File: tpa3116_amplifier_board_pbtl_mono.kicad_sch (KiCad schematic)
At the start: 47 parts, among them IC1 TPA3116D2QDADRQ1, J1 power_supply, J2 Conn_01x04, J3 power_supply, J4 output_right

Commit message: заменил конденсаторы C1, С2 на smd
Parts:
- C1, C2: footprint Capacitor_THT:C_Rect_L7.0mm_W4.5mm_P5.00mm -> Capacitor_SMD:C_0805_2012Metric

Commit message: изменил номинал конденсатора C3
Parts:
- C3: value 1u -> --
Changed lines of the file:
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@@
       (effects (font (size 1.27 1.27)))
     )
-    (property "Value" "1u" (at 58.42 66.04 90)
+    (property "Value" "--" (at 58.42 66.04 90)
       (effects (font (size 1.27 1.27)))
     )

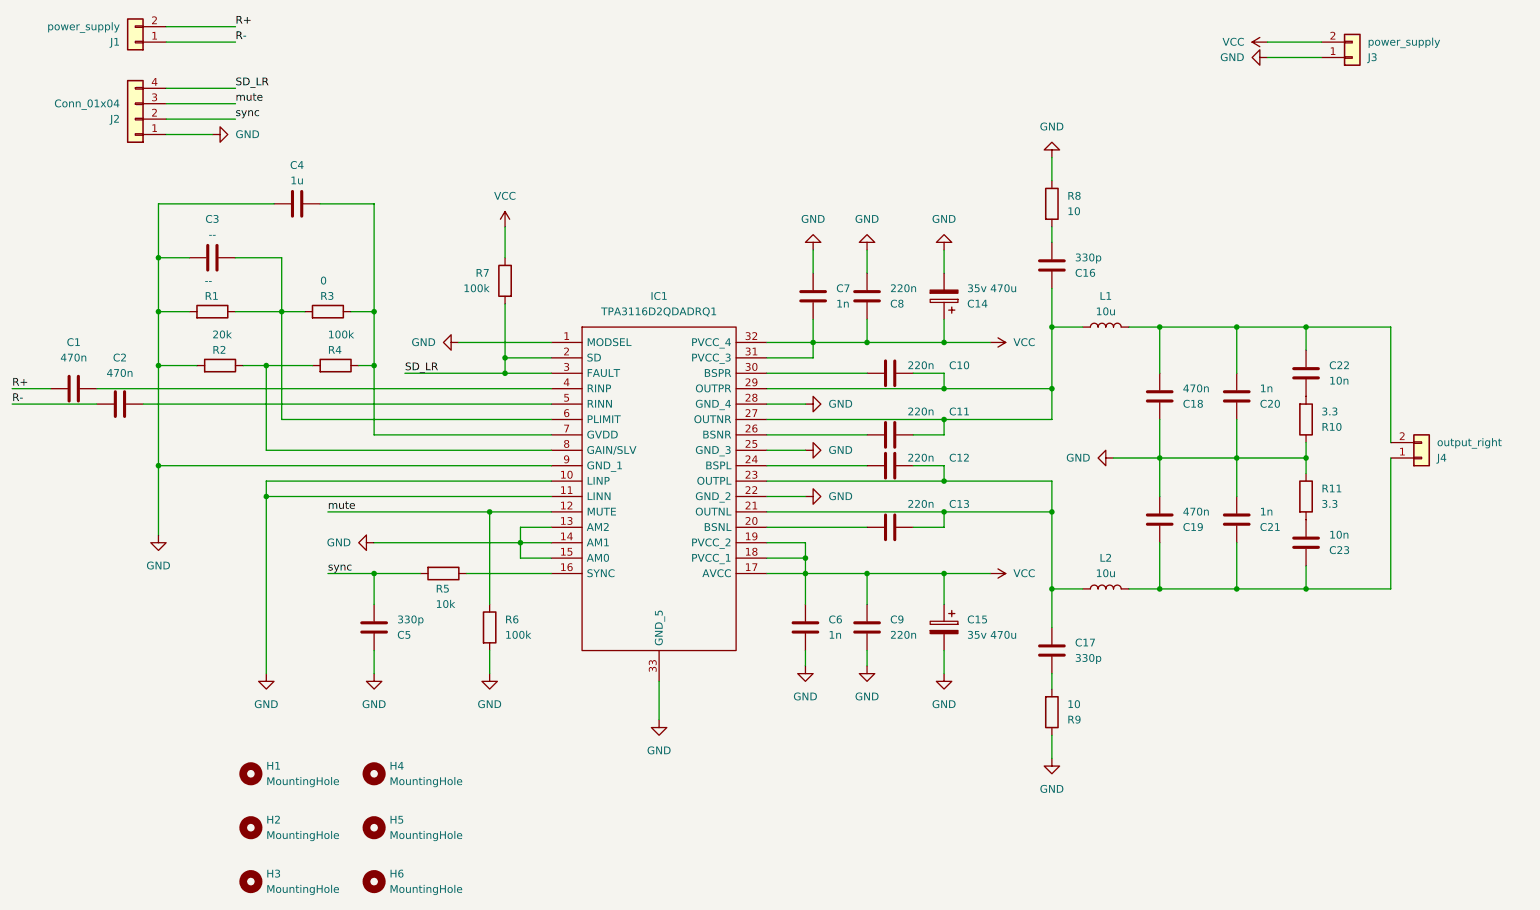
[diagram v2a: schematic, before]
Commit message: Перевернул входные разъемы, изменил номинал конденсаторов входных
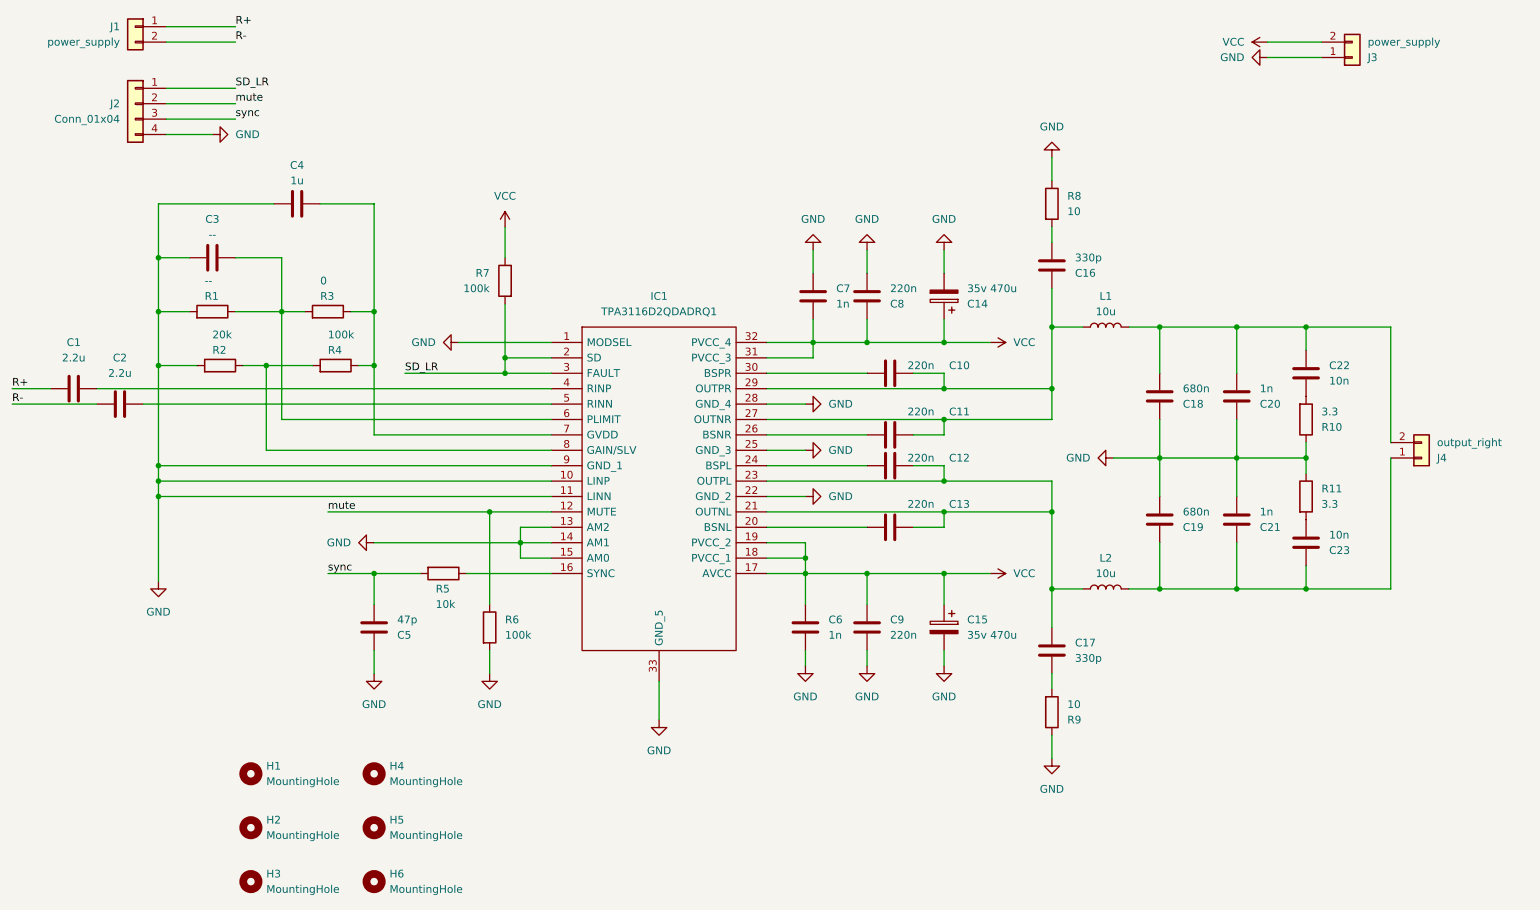
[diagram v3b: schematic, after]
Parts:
- C1, C2: value 470n -> 2.2u
- C18, C19: value 470n -> 680n
- C5: value 330p -> 47p
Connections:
- net GND: now also J2.4 (Pin_4); no longer J2.1 (Pin_1)
- net R+: now also J1.1 (Pin_1); no longer J1.2 (Pin_2)
- net R-: now also J1.2 (Pin_2); no longer J1.1 (Pin_1)
- net SD_LR: now also J2.1 (Pin_1); no longer J2.4 (Pin_4)
- net mute: now also J2.2 (Pin_2); no longer J2.3 (Pin_3)
- net sync: now also J2.3 (Pin_3); no longer J2.2 (Pin_2)
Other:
- moved on the sheet: J1, J2
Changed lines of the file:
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@@
   (junction (at 214.63 81.28) (diameter 0) (color 0 0 0 0)
   )
+  (junction (at 49.53 106.68) (diameter 0) (color 0 0 0 0)
+  )
   (junction (at 238.76 81.28) (diameter 0) (color 0 0 0 0)
   )
@@
   (junction (at 179.07 111.76) (diameter 0) (color 0 0 0 0)
   )
-  (junction (at 67.31 109.22) (diameter 0) (color 0 0 0 0)
+  (junction (at 49.53 109.22) (diameter 0) (color 0 0 0 0)
   )
   (junction (at 104.14 111.76) (diameter 0) (color 0 0 0 0)
@@
     (stroke (width 0) (type default))
   )
+  (wire (pts (xy 49.53 106.68) (xy 49.53 109.22))
+    (stroke (width 0) (type default))
+  )
   (wire (pts (xy 109.22 114.3) (xy 109.22 116.84))
     (stroke (width 0) (type default))
@@
     (stroke (width 0) (type default))
   )
-  (wire (pts (xy 67.31 106.68) (xy 67.31 109.22))
-    (stroke (width 0) (type default))
-  )
   (wire (pts (xy 62.23 41.91) (xy 50.8 41.91))
     (stroke (width 0) (type default))
@@
     (stroke (width 0) (type default))
   )
+  (wire (pts (xy 49.53 109.22) (xy 49.53 123.19))
+    (stroke (width 0) (type default))
+  )
   (wire (pts (xy 49.53 87.63) (xy 55.88 87.63))
     (stroke (width 0) (type default))
@@
     (stroke (width 0) (type default))
   )
-  (wire (pts (xy 49.53 104.14) (xy 49.53 115.57))
+  (wire (pts (xy 49.53 104.14) (xy 49.53 106.68))
     (stroke (width 0) (type default))
   )
@@
     (stroke (width 0) (type default))
   )
-  (wire (pts (xy 67.31 106.68) (xy 114.3 106.68))
+  (wire (pts (xy 49.53 106.68) (xy 114.3 106.68))
     (stroke (width 0) (type default))
   )
@@
     (stroke (width 0) (type default))
   )
+  (wire (pts (xy 49.53 109.22) (xy 114.3 109.22))
+    (stroke (width 0) (type default))
+  )
   (wire (pts (xy 149.86 91.44) (xy 179.07 91.44))
     (stroke (width 0) (type default))
@@
     (stroke (width 0) (type default))
   )
-  (wire (pts (xy 67.31 109.22) (xy 114.3 109.22))
-    (stroke (width 0) (type default))
-  )
   (wire (pts (xy 157.48 83.82) (xy 157.48 86.36))
     (stroke (width 0) (type default))
@@
     (stroke (width 0) (type default))
   )
-  (wire (pts (xy 179.07 138.43) (xy 179.07 134.62))
+  (wire (pts (xy 179.07 137.16) (xy 179.07 134.62))
     (stroke (width 0) (type default))
   )
@@
   )
   (wire (pts (xy 62.23 46.99) (xy 50.8 46.99))
-    (stroke (width 0) (type default))
-  )
-  (wire (pts (xy 67.31 109.22) (xy 67.31 138.43))
     (stroke (width 0) (type default))
   )
@@
     )
   )
-  (symbol (lib_id "Connector_Generic:Conn_01x02") (at 45.72 34.29 180) (unit 1)
-    (in_bom yes) (on_board yes) (dnp no)
-    (property "Reference" "J1" (at 43.18 34.29 0)
-      (effects (font (size 1.27 1.27)) (justify left))
-    )
-    (property "Value" "power_supply" (at 43.18 31.75 0)
-      (effects (font (size 1.27 1.27)) (justify left))
-    )
-    (property "Footprint" "Connector_JST:JST_EH_B2B-EH-A_1x02_P2.50mm_Vertical" (at 45.72 34.29 0)
-      (effects (font (size 1.27 1.27)) hide)
-    )
-    (property "Datasheet" "~" (at 45.72 34.29 0)
+  (symbol (lib_id "Connector_Generic:Conn_01x02") (at 45.72 31.75 0) (mirror y) (unit 1)
+    (in_bom yes) (on_board yes) (dnp no)
+    (property "Reference" "J1" (at 43.18 31.75 0)
+      (effects (font (size 1.27 1.27)) (justify left))
+    )
+    (property "Value" "power_supply" (at 43.18 34.29 0)
+      (effects (font (size 1.27 1.27)) (justify left))
+    )
+    (property "Footprint" "Connector_JST:JST_EH_B2B-EH-A_1x02_P2.50mm_Vertical" (at 45.72 31.75 0)
+      (effects (font (size 1.27 1.27)) hide)
+    )
+    (property "Datasheet" "~" (at 45.72 31.75 0)
       (effects (font (size 1.27 1.27)) hide)
     )
@@
     )
   )
-  (symbol (lib_id "power:GND") (at 67.31 138.43 0) (unit 1)
-    (in_bom yes) (on_board yes) (dnp no) (fields_autoplaced)
-    (property "Reference" "#PWR03" (at 67.31 144.78 0)
-      (effects (font (size 1.27 1.27)) hide)
-    )
-    (property "Value" "GND" (at 67.31 143.51 0)
-      (effects (font (size 1.27 1.27)))
-    )
-    (property "Footprint" "" (at 67.31 138.43 0)
-      (effects (font (size 1.27 1.27)) hide)
-    )
-    (property "Datasheet" "" (at 67.31 138.43 0)
-      (effects (font (size 1.27 1.27)) hide)
-    )
-    (pin "1")
-    (instances
-      (project "tpa3116_amplifier_board_pbtl_mono"
-        (path "/d7856d41-bcae-4bc4-ad9f-ba9483713084"
-          (reference "#PWR03") (unit 1)
-        )
-      )
-    )
-  )
   (symbol (lib_id "Device:C") (at 196.85 134.62 0) (unit 1)
     (in_bom yes) (on_board yes) (dnp no) (fields_autoplaced)
@@
     )
   )
-  (symbol (lib_id "power:GND") (at 49.53 115.57 0) (unit 1)
-    (in_bom yes) (on_board yes) (dnp no) (fields_autoplaced)
-    (property "Reference" "#PWR01" (at 49.53 121.92 0)
-      (effects (font (size 1.27 1.27)) hide)
-    )
-    (property "Value" "GND" (at 49.53 120.65 0)
-      (effects (font (size 1.27 1.27)))
-    )
-    (property "Footprint" "" (at 49.53 115.57 0)
-      (effects (font (size 1.27 1.27)) hide)
-    )
-    (property "Datasheet" "" (at 49.53 115.57 0)
+  (symbol (lib_id "power:GND") (at 49.53 123.19 0) (unit 1)
+    (in_bom yes) (on_board yes) (dnp no) (fields_autoplaced)
+    (property "Reference" "#PWR01" (at 49.53 129.54 0)
+      (effects (font (size 1.27 1.27)) hide)
+    )
+    (property "Value" "GND" (at 49.53 128.27 0)
+      (effects (font (size 1.27 1.27)))
+    )
+    (property "Footprint" "" (at 49.53 123.19 0)
+      (effects (font (size 1.27 1.27)) hide)
+    )
+    (property "Datasheet" "" (at 49.53 123.19 0)
       (effects (font (size 1.27 1.27)) hide)
     )
@@
       (effects (font (size 1.27 1.27)) (justify left))
     )
-    (property "Value" "470n" (at 218.44 91.44 0)
+    (property "Value" "680n" (at 218.44 91.44 0)
       (effects (font (size 1.27 1.27)) (justify left))
     )
@@
     )
   )
-  (symbol (lib_id "power:GND") (at 179.07 138.43 0) (unit 1)
-    (in_bom yes) (on_board yes) (dnp no) (fields_autoplaced)
-    (property "Reference" "#PWR018" (at 179.07 144.78 0)
-      (effects (font (size 1.27 1.27)) hide)
-    )
-    (property "Value" "GND" (at 179.07 143.51 0)
-      (effects (font (size 1.27 1.27)))
-    )
-    (property "Footprint" "" (at 179.07 138.43 0)
-      (effects (font (size 1.27 1.27)) hide)
-    )
-    (property "Datasheet" "" (at 179.07 138.43 0)
+  (symbol (lib_id "power:GND") (at 179.07 137.16 0) (unit 1)
+    (in_bom yes) (on_board yes) (dnp no) (fields_autoplaced)
+    (property "Reference" "#PWR018" (at 179.07 143.51 0)
+      (effects (font (size 1.27 1.27)) hide)
+    )
+    (property "Value" "GND" (at 179.07 142.24 0)
+      (effects (font (size 1.27 1.27)))
+    )
+    (property "Footprint" "" (at 179.07 137.16 0)
+      (effects (font (size 1.27 1.27)) hide)
+    )
+    (property "Datasheet" "" (at 179.07 137.16 0)
       (effects (font (size 1.27 1.27)) hide)
     )
@@
       (effects (font (size 1.27 1.27)))
     )
-    (property "Value" "470n" (at 35.56 86.36 90)
+    (property "Value" "2.2u" (at 35.56 86.36 90)
       (effects (font (size 1.27 1.27)))
     )
@@
     )
   )
-  (symbol (lib_id "Connector_Generic:Conn_01x04") (at 45.72 46.99 180) (unit 1)
-    (in_bom yes) (on_board yes) (dnp no)
-    (property "Reference" "J2" (at 43.18 46.99 0)
-      (effects (font (size 1.27 1.27)) (justify left))
-    )
-    (property "Value" "Conn_01x04" (at 43.18 44.45 0)
-      (effects (font (size 1.27 1.27)) (justify left))
-    )
-    (property "Footprint" "Connector_JST:JST_EH_B4B-EH-A_1x04_P2.50mm_Vertical" (at 45.72 46.99 0)
-      (effects (font (size 1.27 1.27)) hide)
-    )
-    (property "Datasheet" "~" (at 45.72 46.99 0)
+  (symbol (lib_id "Connector_Generic:Conn_01x04") (at 45.72 44.45 0) (mirror y) (unit 1)
+    (in_bom yes) (on_board yes) (dnp no)
+    (property "Reference" "J2" (at 43.18 44.45 0)
+      (effects (font (size 1.27 1.27)) (justify left))
+    )
+    (property "Value" "Conn_01x04" (at 43.18 46.99 0)
+      (effects (font (size 1.27 1.27)) (justify left))
+    )
+    (property "Footprint" "Connector_JST:JST_EH_B4B-EH-A_1x04_P2.50mm_Vertical" (at 45.72 44.45 0)
+      (effects (font (size 1.27 1.27)) hide)
+    )
+    (property "Datasheet" "~" (at 45.72 44.45 0)
       (effects (font (size 1.27 1.27)) hide)
     )
@@
       (effects (font (size 1.27 1.27)) (justify left))
     )
-    (property "Value" "330p" (at 88.9 129.54 0)
+    (property "Value" "47p" (at 88.9 129.54 0)
       (effects (font (size 1.27 1.27)) (justify left))
     )
@@
       (effects (font (size 1.27 1.27)))
     )
-    (property "Value" "470n" (at 43.18 88.9 90)
+    (property "Value" "2.2u" (at 43.18 88.9 90)
       (effects (font (size 1.27 1.27)))
     )
@@
       (effects (font (size 1.27 1.27)) (justify left))
     )
-    (property "Value" "470n" (at 218.44 111.76 0)
-      (effects (font (size 1.27 1.27)) (justify left))
-    )
+    (property "Value" "680n" (at 218.44 111.76 0)
+      (effects (font (size 1.27 1.27)) (justify left))
+    )

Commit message: заменил входные разъемы на PH 2.0
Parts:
- J1: footprint Connector_JST:JST_EH_B2B-EH-A_1x02_P2.50mm_Vertical -> Connector_JST:JST_PH_B2B-PH-K_1x02_P2.00mm_Vertical
- J2: footprint Connector_JST:JST_EH_B4B-EH-A_1x04_P2.50mm_Vertical -> Connector_JST:JST_PH_B4B-PH-K_1x04_P2.00mm_Vertical
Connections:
- net GND: now also J2.1 (Pin_1); no longer J2.4 (Pin_4)
- net R+: now also J1.2 (Pin_2); no longer J1.1 (Pin_1)
- net R-: now also J1.1 (Pin_1); no longer J1.2 (Pin_2)
- net SD_LR: now also J2.4 (Pin_4); no longer J2.1 (Pin_1)
- net mute: now also J2.3 (Pin_3); no longer J2.2 (Pin_2)
- net sync: now also J2.2 (Pin_2); no longer J2.3 (Pin_3)
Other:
- moved on the sheet: J1, J2
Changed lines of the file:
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@@
     )
   )
-  (symbol (lib_id "Connector_Generic:Conn_01x02") (at 45.72 31.75 0) (mirror y) (unit 1)
-    (in_bom yes) (on_board yes) (dnp no)
-    (property "Reference" "J1" (at 43.18 31.75 0)
-      (effects (font (size 1.27 1.27)) (justify left))
-    )
-    (property "Value" "power_supply" (at 43.18 34.29 0)
-      (effects (font (size 1.27 1.27)) (justify left))
-    )
-    (property "Footprint" "Connector_JST:JST_EH_B2B-EH-A_1x02_P2.50mm_Vertical" (at 45.72 31.75 0)
-      (effects (font (size 1.27 1.27)) hide)
-    )
-    (property "Datasheet" "~" (at 45.72 31.75 0)
+  (symbol (lib_id "Connector_Generic:Conn_01x02") (at 45.72 34.29 180) (unit 1)
+    (in_bom yes) (on_board yes) (dnp no)
+    (property "Reference" "J1" (at 43.18 34.29 0)
+      (effects (font (size 1.27 1.27)) (justify left))
+    )
+    (property "Value" "power_supply" (at 43.18 31.75 0)
+      (effects (font (size 1.27 1.27)) (justify left))
+    )
+    (property "Footprint" "Connector_JST:JST_PH_B2B-PH-K_1x02_P2.00mm_Vertical" (at 45.72 34.29 0)
+      (effects (font (size 1.27 1.27)) hide)
+    )
+    (property "Datasheet" "~" (at 45.72 34.29 0)
       (effects (font (size 1.27 1.27)) hide)
     )
@@
     )
   )
-  (symbol (lib_id "Connector_Generic:Conn_01x04") (at 45.72 44.45 0) (mirror y) (unit 1)
-    (in_bom yes) (on_board yes) (dnp no)
-    (property "Reference" "J2" (at 43.18 44.45 0)
-      (effects (font (size 1.27 1.27)) (justify left))
-    )
-    (property "Value" "Conn_01x04" (at 43.18 46.99 0)
-      (effects (font (size 1.27 1.27)) (justify left))
-    )
-    (property "Footprint" "Connector_JST:JST_EH_B4B-EH-A_1x04_P2.50mm_Vertical" (at 45.72 44.45 0)
-      (effects (font (size 1.27 1.27)) hide)
-    )
-    (property "Datasheet" "~" (at 45.72 44.45 0)
-      (effects (font (size 1.27 1.27)) hide)
-    )
+  (symbol (lib_id "Connector_Generic:Conn_01x04") (at 45.72 46.99 180) (unit 1)
+    (in_bom yes) (on_board yes) (dnp no)
+    (property "Reference" "J2" (at 43.18 46.99 0)
+      (effects (font (size 1.27 1.27)) (justify left))
+    )
+    (property "Value" "Conn_01x04" (at 43.18 44.45 0)
+      (effects (font (size 1.27 1.27)) (justify left))
+    )
+    (property "Footprint" "Connector_JST:JST_PH_B4B-PH-K_1x04_P2.00mm_Vertical" (at 45.72 46.99 0)
+      (effects (font (size 1.27 1.27)) hide)
+    )
+    (property "Datasheet" "~" (at 45.72 46.99 0)
+      (effects (font (size 1.27 1.27)) hide)
+    )
